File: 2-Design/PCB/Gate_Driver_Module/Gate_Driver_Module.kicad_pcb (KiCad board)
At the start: 2 copper layers, 8 parts, among them U1 ROE-0512S, U2 LTV-817, U3 TC4421

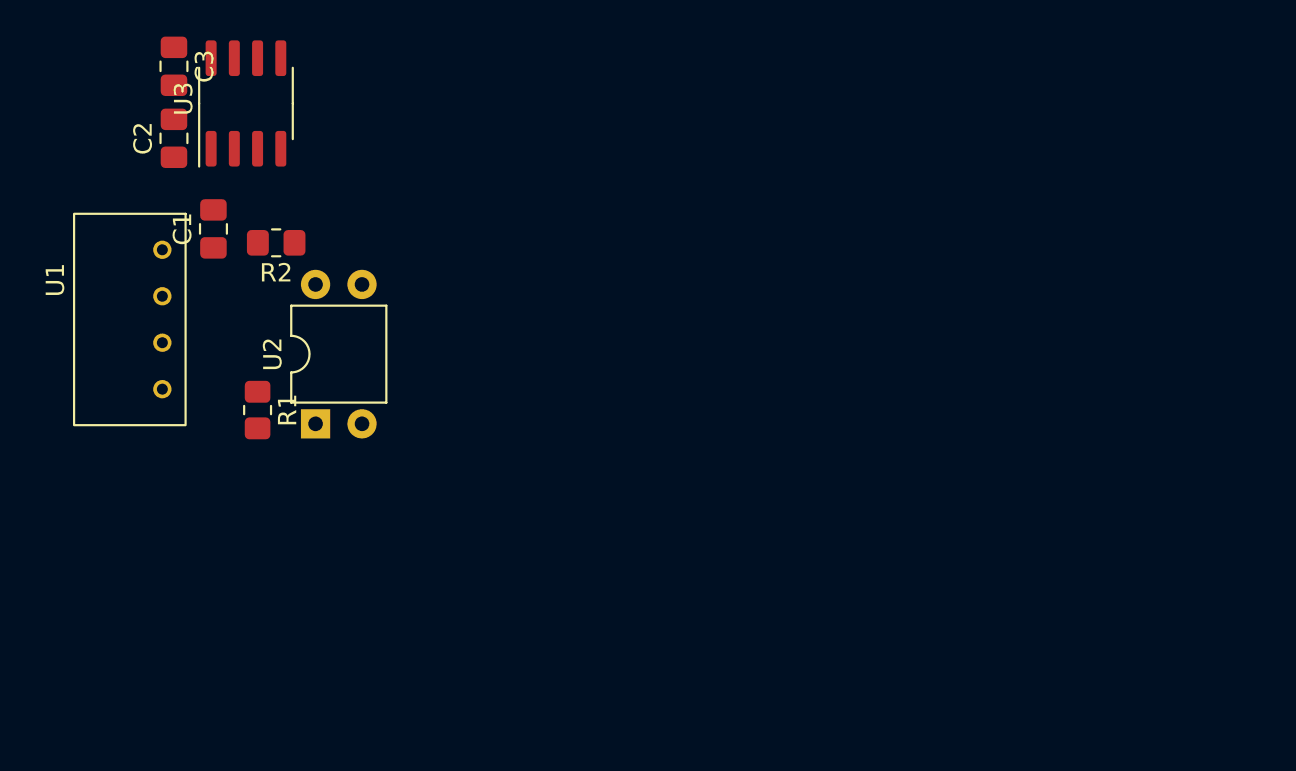
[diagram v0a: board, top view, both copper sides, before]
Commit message: Gate Driver Module placements somewhat ready, to be drawn
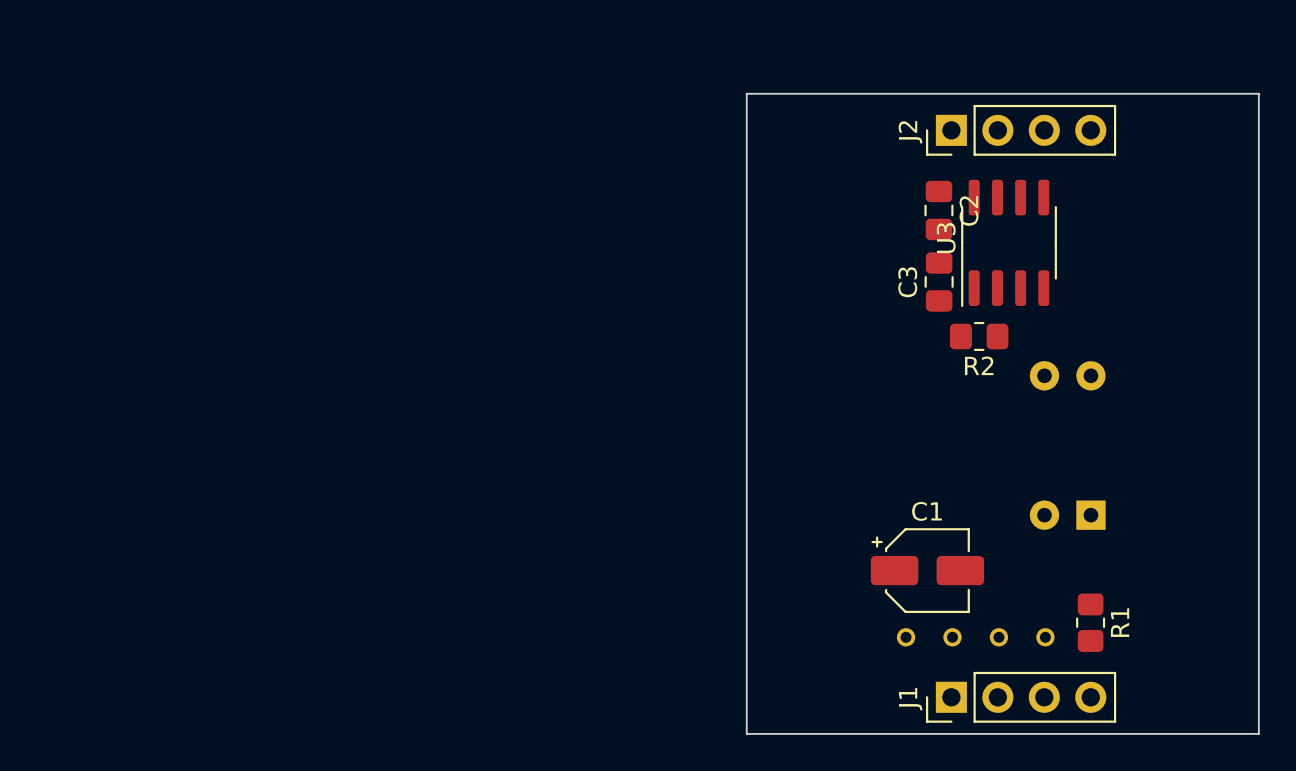
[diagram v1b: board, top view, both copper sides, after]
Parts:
- added J1: Conn_01x04_Male, Connector_PinHeader_2.54mm:PinHeader_1x04_P2.54mm_Vertical, F.Cu at (173.2, 113.8)
- added J2: Conn_01x04_Male, Connector_PinHeader_2.54mm:PinHeader_1x04_P2.54mm_Vertical, F.Cu at (173.2, 82.8)
- C1: footprint Capacitor_SMD:C_0805_2012Metric_Pad1.18x1.45mm_HandSolder -> Capacitor_SMD:CP_Elec_4x5.4
- U1, U2: moved to B.Cu
- U3: value TC4421 -> TC4421A
- moved U1 47.7 mm to (174.5, 110.5), turned to 180 degrees
- moved R1 47.0 mm to (180.8, 109.7)
- moved C3 43.5 mm to (172.5, 91.0), turned to 90 degrees
- moved C1 43.3 mm to (171.9, 106.8), turned to 0 degrees
- moved U2 42.7 mm to (180.8, 103.8)
- moved U3 42.4 mm to (176.3, 88.9)
- moved C2 42.0 mm to (172.5, 87.1), turned to -90 degrees
- moved R2 38.8 mm to (174.7, 94.0)
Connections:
- C1 pad 1: Net-(C1-Pad1) -> Net-(C3-Pad1)
- C2 pad 1: Net-(C1-Pad1) -> Net-(C3-Pad1)
- R1 pad 2: Q1_PWM -> Q_PWM
- R2 pad 2: Net-(C1-Pad1) -> Net-(C3-Pad1)
- U1 pad 4: Net-(C1-Pad1) -> Net-(C3-Pad1)
- U3 pad 1: Net-(C1-Pad1) -> Net-(C3-Pad1)
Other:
- board outline added: 28 x 35 mm

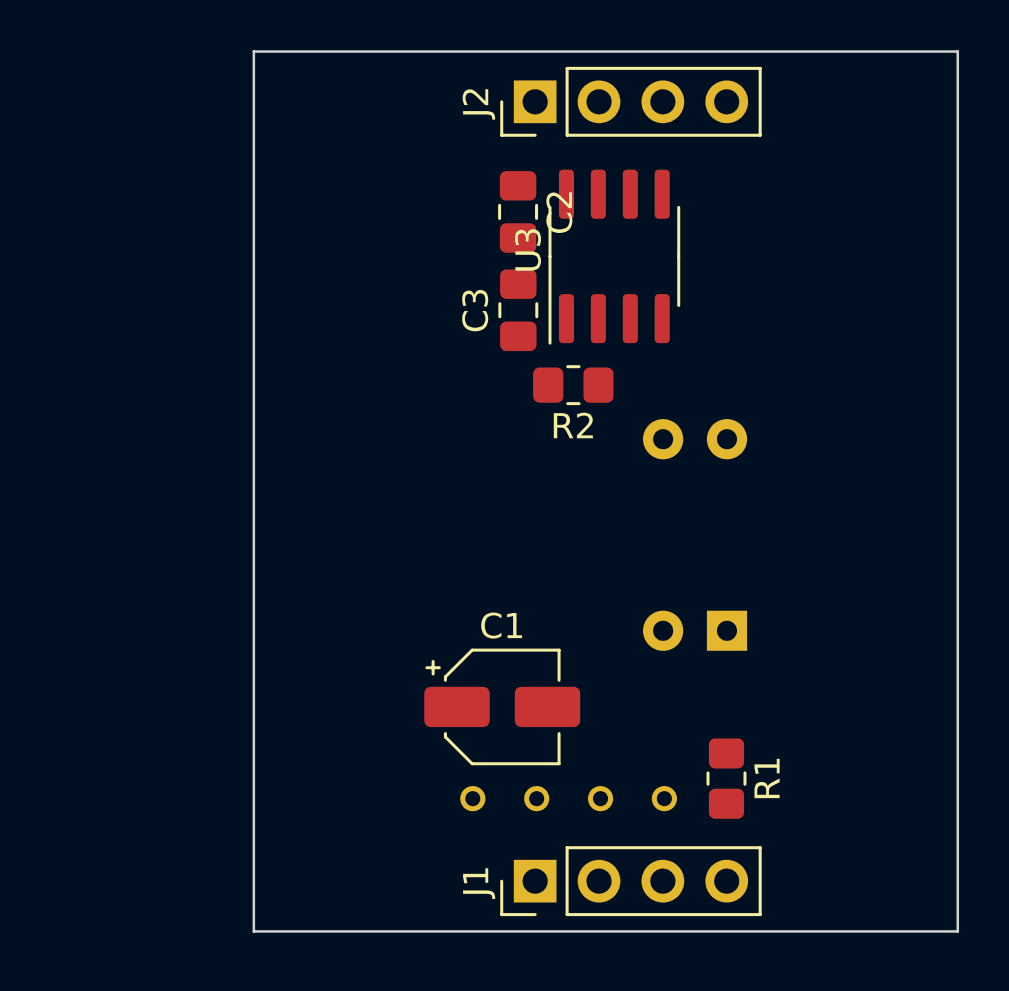
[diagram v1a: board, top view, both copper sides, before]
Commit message: Gate Driver Module placements are not somewhat ready, but it takes time for isik to learn
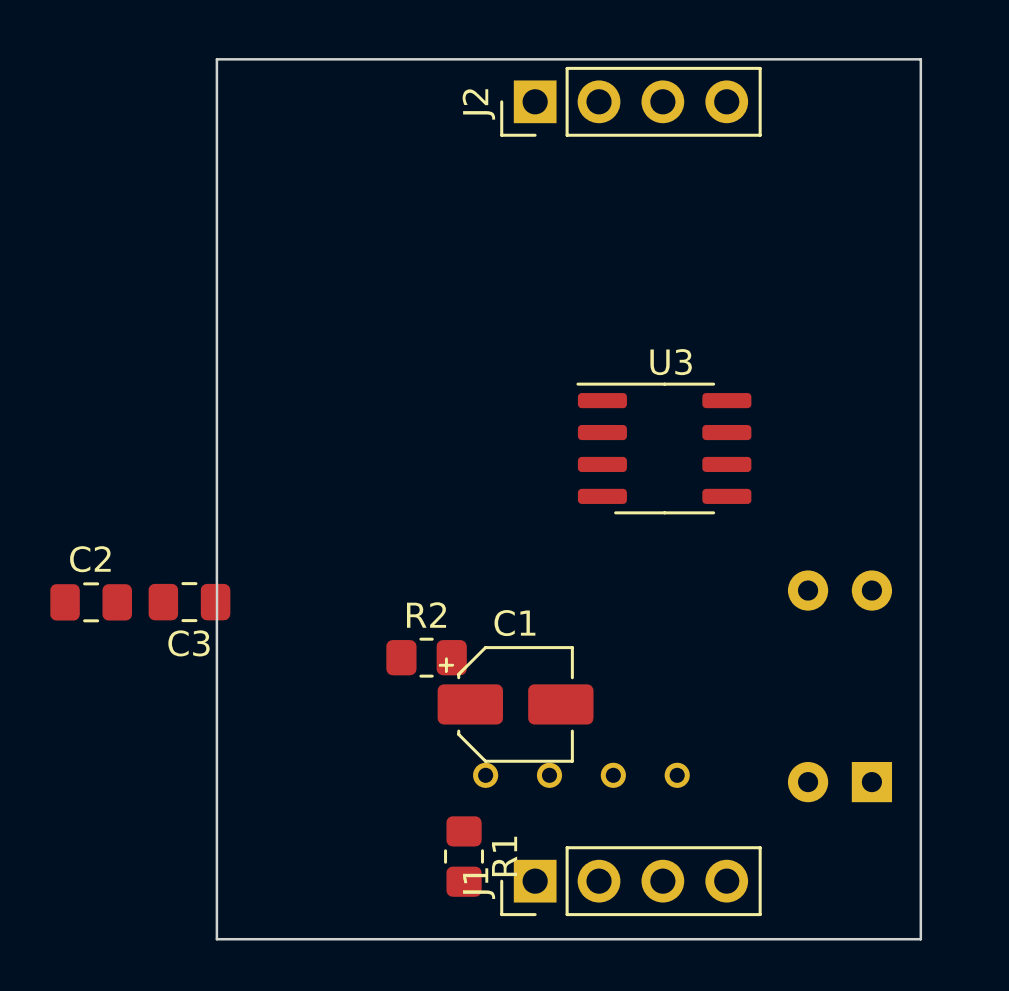
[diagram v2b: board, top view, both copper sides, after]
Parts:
- moved C2 23.0 mm to (155.5, 102.7), turned to 0 degrees
- moved C3 17.5 mm to (159.4, 102.7), turned to 180 degrees
- moved R2 12.3 mm to (168.9, 104.9), turned to 0 degrees
- moved R1 10.9 mm to (170.4, 112.8)
- moved U2 8.34 mm to (186.6, 109.8)
- moved U3 7.90 mm to (178.3, 96.5), turned to 0 degrees
- moved U1 1.06 mm to (175.0, 109.5)
- moved C1 0.54 mm to (172.4, 106.7)
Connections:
- J1 pad 1: unconnected-(J1-Pad1) -> Q_PWM
- J1 pad 2: +5V -> GND
- J1 pad 3: GND -> +5V
- J1 pad 4: Q_PWM -> unconnected-(J1-Pad4)

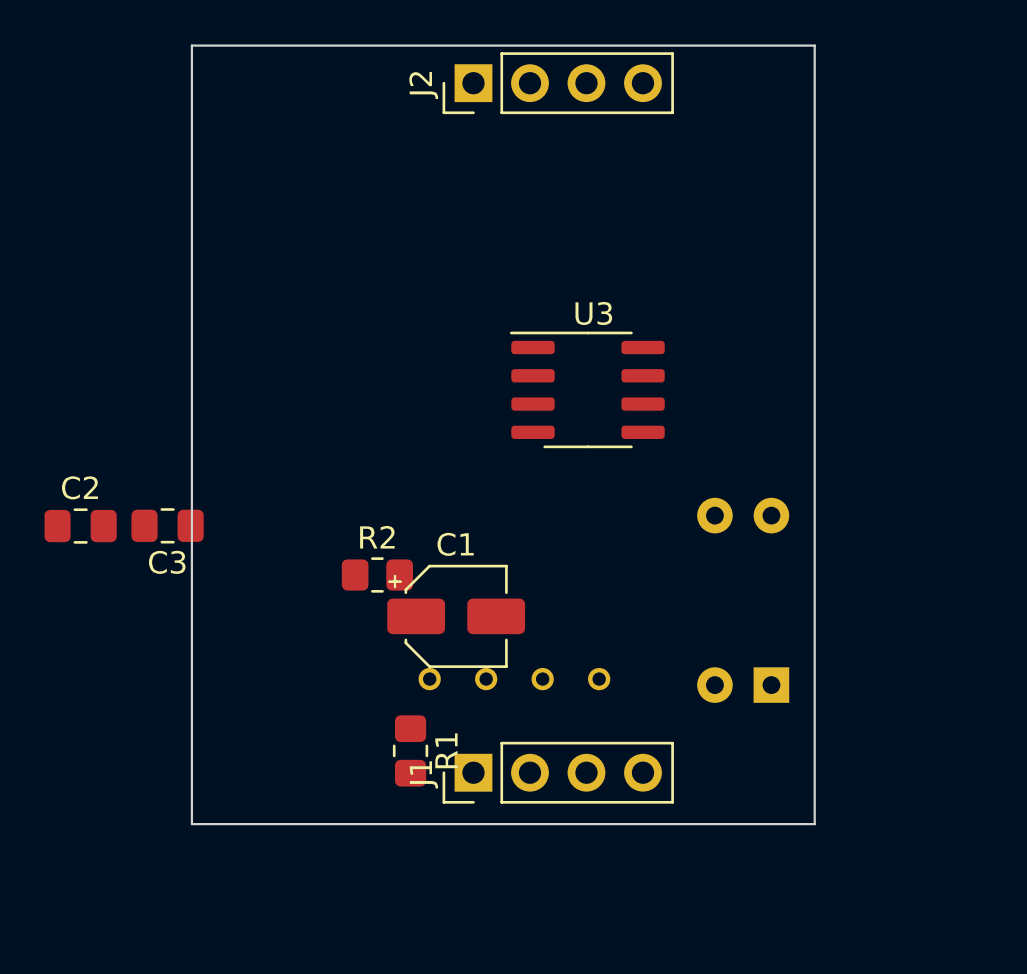
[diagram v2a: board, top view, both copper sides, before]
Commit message: Gate Driver Module v1 completed, minor polishing to be done
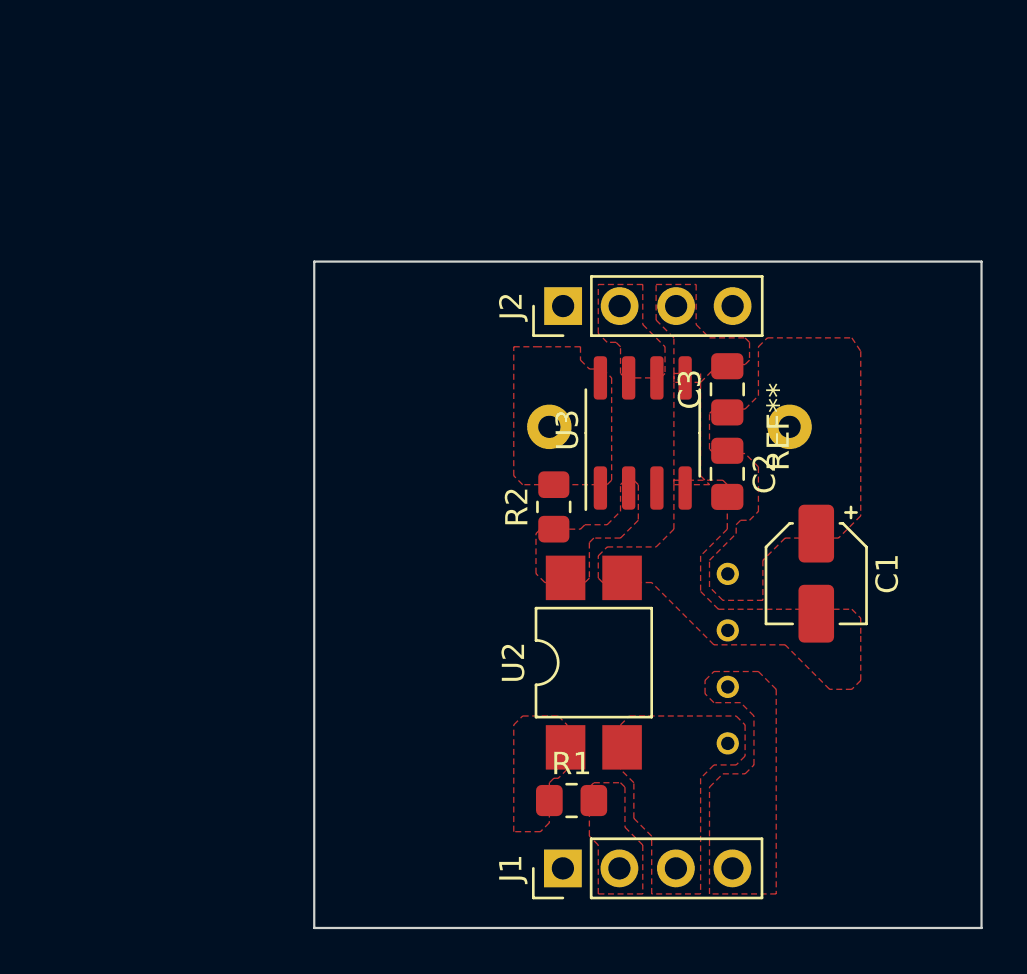
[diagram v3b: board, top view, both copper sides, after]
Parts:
- added ?: , , F.Cu at (176.6, 98.2)
- added REF**: Jumper_Wire_Hole, ee463_footprint_lib:Jumper_Wire_Hole, F.Cu at (187.4, 98.2)
- U2: footprint Package_DIP:DIP-4_W7.62mm -> Package_DIP:SMDIP-4_W7.62mm; moved to F.Cu
- moved C2 29.2 mm to (184.6, 100.3), turned to -90 degrees
- moved C3 25.9 mm to (184.6, 96.5), turned to 90 degrees
- moved C1 16.3 mm to (188.6, 104.8), turned to -90 degrees
- moved J2 10.8 mm to (177.2, 92.8)
- moved U1 9.64 mm to (184.6, 108.6), turned to 90 degrees
- moved R2 8.50 mm to (176.8, 101.8), turned to 90 degrees
- moved U2 8.05 mm to (178.6, 108.8)
- moved R1 7.58 mm to (177.6, 115.0), turned to 0 degrees
- moved J1 5.89 mm to (177.2, 118.0)
- moved U3 3.13 mm to (180.8, 98.5), turned to 90 degrees
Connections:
- J1 pad 1: Q_PWM -> unconnected-(J1-Pad1)
- J1 pad 2: GND -> Q_PWM
- J1 pad 3: +5V -> GND
- J1 pad 4: unconnected-(J1-Pad4) -> +5V
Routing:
- added copper zone on F.Cu, net +5V
- added copper zone on F.Cu, net GND
- added copper zone on F.Cu, net GND_12
- added copper zone on F.Cu, net Net-(C1-Pad1)
- added copper zone on F.Cu, net Net-(R1-Pad1)
- added copper zone on F.Cu, net Net-(R2-Pad1)
- added copper zone on F.Cu, net QG
- added copper zone on F.Cu, net Q_PWM
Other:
- board size 28 x 35 mm -> 30 x 30 mm

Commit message: Gate Driver Module v1 completed
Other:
- board text added: "EE463 - 2022 Fall"
- board text added: "Fatih Erden"
- board text added: "Four Quad DC Motor Driver"
- board text added: "Işık Altunkol"
- board text added: "İsmail Macit"
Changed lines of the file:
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@@
   )
   (gr_rect (start 166.03 90.77) (end 196.03 120.73) (layer "Edge.Cuts") (width 0.1) (fill none))
+  (gr_text "İsmail Macit" (at 170.7 108.5 270) (layer "F.Cu")
+    (effects (font (size 0.75 0.75) (thickness 0.15)) (justify left))
+  )
+  (gr_text "Fatih Erden" (at 172.2 108.5 270) (layer "F.Cu")
+    (effects (font (size 0.75 0.75) (thickness 0.15)) (justify left))
+  )
+  (gr_text "Işık Altunkol" (at 169.2 108.5 270) (layer "F.Cu")
+    (effects (font (size 0.75 0.75) (thickness 0.15)) (justify left))
+  )
+  (gr_text "EE463 - 2022 Fall " (at 171 94.7 270) (layer "F.Cu")
+    (effects (font (size 0.65 0.65) (thickness 0.15)) (justify left))
+  )
+  (gr_text "Four Quad DC Motor Driver" (at 170.1 95.4 270) (layer "F.Cu")
+    (effects (font (size 0.4 0.4) (thickness 0.1)) (justify left))
+  )
   (zone (net 10) (net_name "QG") (layer "F.Cu") (hatch edge 0.508)
     (connect_pads yes (clearance 0.508))
@@
     (polygon
       (pts
-        (xy 180.8 93.6)
-        (xy 181.8 94.6)
-        (xy 181.8 95.8)
-        (xy 181.6 96)
+        (xy 180.8 94.2)
+        (xy 181.6 94.9)
+        (xy 181.6 95.8)
+        (xy 181.4 96)
         (xy 180.6 96)
         (xy 180.4 96)
@@
     (polygon
       (pts
-        (xy 186.8 110)
-        (xy 186.8 119.2)
-        (xy 183.8 119.2)
-        (xy 183.8 114.4)
-        (xy 184.4 113.8)
-        (xy 185.4 113.8)
-        (xy 185.8 113.4)
-        (xy 185.8 111.2)
-        (xy 185.2 110.6)
+        (xy 187.2 110.4)
+        (xy 187.2 119.2)
+        (xy 184 119.2)
+        (xy 184 116.8)
+        (xy 184.6 116.2)
+        (xy 184.6 114.4)
+        (xy 185 114)
+        (xy 185.6 114)
+        (xy 186 113.4)
+        (xy 186 111.2)
+        (xy 185.4 110.6)
         (xy 184 110.6)
         (xy 183.6 110.2)
@@
     (polygon
       (pts
-        (xy 185.4 111.6)
-        (xy 185.4 113)
-        (xy 185 113.4)
-        (xy 184 113.4)
+        (xy 185.2 111.8)
+        (xy 185.2 112.8)
+        (xy 184.8 113.2)
+        (xy 184.2 113.2)
         (xy 183.4 114)
         (xy 183.4 119.2)
-        (xy 181.2 119.2)
-        (xy 181.2 116.6)
-        (xy 180.4 115.8)
+        (xy 181.4 119.2)
+        (xy 181.4 116.6)
+        (xy 180.4 115.6)
         (xy 180.4 114.2)
         (xy 179.8 113.6)
-        (xy 179.8 111.6)
-        (xy 180.2 111.2)
-        (xy 185 111.2)
+        (xy 179.8 111.8)
+        (xy 180.2 111.4)
+        (xy 184.8 111.4)
       )
     )
@@
     (polygon
       (pts
-        (xy 190.6 94.8)
+        (xy 190.6 94.6)
         (xy 190.6 102.2)
         (xy 189.6 103.2)
         (xy 187.2 103.2)
         (xy 186.2 104.2)
-        (xy 186.2 106)
-        (xy 184.4 106)
-        (xy 183.8 105.4)
-        (xy 183.8 104.2)
-        (xy 185 103)
-        (xy 185 102.6)
-        (xy 185.2 102.4)
-        (xy 185.6 102.4)
-        (xy 186 102)
+        (xy 186.2 105.4)
+        (xy 186.2 105.8)
+        (xy 184.6 105.8)
+        (xy 184 105.2)
+        (xy 184 104.2)
+        (xy 186 102.2)
         (xy 186 100)
         (xy 185.4 99.4)
-        (xy 184 99.4)
-        (xy 183.8 99.2)
-        (xy 183.8 97.6)
-        (xy 184 97.4)
+        (xy 184.4 99.4)
+        (xy 184.2 99.2)
+        (xy 184.2 97.6)
+        (xy 184.4 97.4)
         (xy 185.4 97.4)
-        (xy 186 96.8)
-        (xy 186 94.6)
-        (xy 186.4 94.2)
-        (xy 190.2 94.2)
+        (xy 186.2 96.6)
+        (xy 186.2 95)
+        (xy 186.6 94.6)
+        (xy 190.2 94.6)
       )
     )
@@
     (polygon
       (pts
-        (xy 183.4 100.4)
-        (xy 183.8 100.8)
+        (xy 183.2 100.4)
+        (xy 183.4 100.6)
         (xy 182.2 100.8)
         (xy 182.2 95.8)
-        (xy 183.4 95.8)
+        (xy 183.2 95.8)
       )
     )
@@
       (pts
         (xy 180.6 100.8)
-        (xy 180.6 102.4)
-        (xy 179.8 103.2)
+        (xy 180.6 102.6)
+        (xy 180 103.2)
         (xy 178.6 103.2)
         (xy 178.4 103.4)
@@
         (xy 176 103)
         (xy 176.2 102.8)
-        (xy 178 102.8)
-        (xy 178.2 102.6)
-        (xy 179.2 102.6)
-        (xy 179.8 102)
+        (xy 177.8 102.8)
+        (xy 178 102.6)
+        (xy 179.4 102.6)
+        (xy 179.8 102.2)
         (xy 179.8 100.8)
         (xy 180 100.6)
@@
     (polygon
       (pts
-        (xy 184.6 100.8)
-        (xy 184.6 102.8)
-        (xy 183.4 104)
-        (xy 183.4 105.6)
-        (xy 184.2 106.4)
-        (xy 190.2 106.4)
+        (xy 184.4 100.8)
+        (xy 184.4 102.4)
+        (xy 183 103.8)
+        (xy 183 105.6)
+        (xy 184 106.6)
+        (xy 190.2 106.6)
         (xy 190.6 106.8)
         (xy 190.6 107.6)
@@
         (xy 189.2 110)
         (xy 187.2 108)
-        (xy 184 108)
+        (xy 183 108)
+        (xy 182.2 108)
+        (xy 181.6 107.4)
+        (xy 181.6 105.6)
         (xy 181.2 105.2)
-        (xy 179 105.2)
-        (xy 178.8 105)
-        (xy 178.8 104)
-        (xy 179.2 103.6)
-        (xy 181.4 103.6)
-        (xy 182.2 102.8)
+        (xy 179.2 105.2)
+        (xy 179 105)
+        (xy 179 104)
+        (xy 179.4 103.8)
+        (xy 181.4 103.8)
+        (xy 182.2 103)
         (xy 182.2 100.6)
         (xy 182.4 100.6)
@@
       (pts
         (xy 183.2 93.6)
-        (xy 183.8 94.2)
-        (xy 185.4 94.2)
-        (xy 185.6 94.4)
-        (xy 185.6 95.2)
-        (xy 185.4 95.4)
+        (xy 184 94.4)
+        (xy 185.2 94.4)
+        (xy 185.4 94.6)
+        (xy 185.4 95.2)
+        (xy 185.2 95.4)
         (xy 184.2 95.4)
         (xy 183.4 96.2)
@@
     (polygon
       (pts
-        (xy 180 114.4)
-        (xy 180 116.2)
+        (xy 179.6 114.6)
+        (xy 179.6 116.4)
+        (xy 180 116.8)
+        (xy 180.6 116.8)
         (xy 180.8 117)
         (xy 180.8 119.2)
@@
         (xy 178.8 117)
         (xy 178.4 116.6)
-        (xy 178.4 114.4)
-        (xy 178.6 114.2)
-        (xy 179.8 114.2)
+        (xy 178.4 114.6)
+        (xy 178.6 114.4)
+        (xy 179.4 114.4)
       )
     )
@@
     (polygon
       (pts
-        (xy 179.4 96)
-        (xy 179.4 100.6)
-        (xy 179.2 100.8)
+        (xy 179.2 96)
+        (xy 179.2 100.6)
+        (xy 178.8 100.8)
         (xy 175.4 100.8)
         (xy 175 100.4)
@@
         (xy 178 95.2)
         (xy 178.4 95.6)
-        (xy 179 95.6)
+        (xy 178.8 95.6)
       )
     )
@@
         (xy 176.6 114.2)
         (xy 176.6 116)
-        (xy 176.2 116.4)
-        (xy 175 116.4)
+        (xy 176.4 116.2)
+        (xy 175 116.2)
         (xy 175 111.6)
         (xy 175.4 111.2)
